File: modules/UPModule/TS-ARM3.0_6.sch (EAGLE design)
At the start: 82 parts, among them IC1 LPC1115, IC100 BD9G101, P1 , P10 , P11 , P12 , P13 , P14 , P2 , P3 , P4 , P5 , P6 , P7 , P8 , P9 , Q1 FA-20H, T1 BC856, T2 BCP52, T3 BC847, X1 EIB

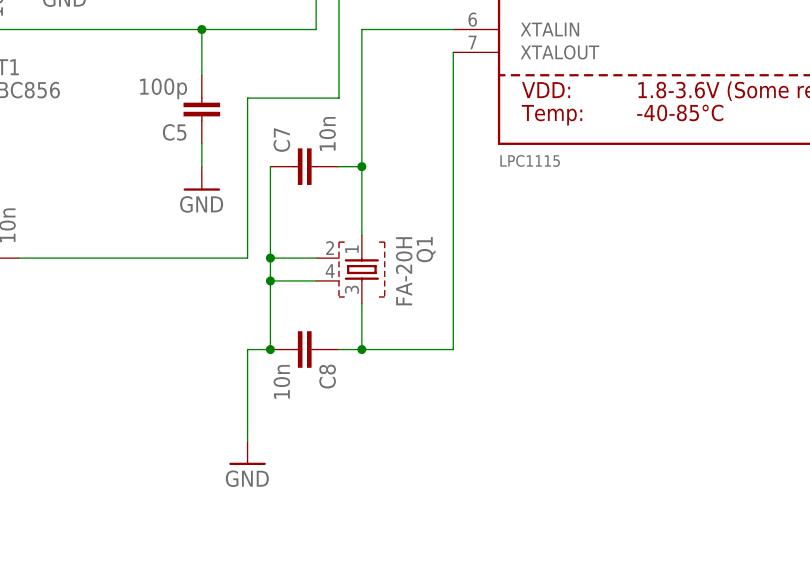
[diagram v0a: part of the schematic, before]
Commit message: Quarz footprint auf ASF geändert
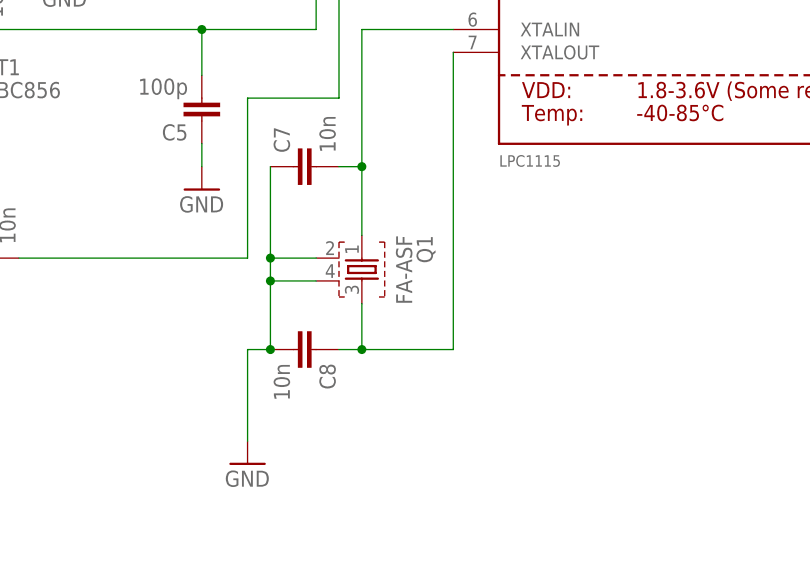
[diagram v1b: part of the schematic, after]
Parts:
- Q1: value FA-20H -> FA-ASF; device crystal:FA-20H -> crystal:FA-ASF
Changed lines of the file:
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@@
 <part name="C7" library="rcl" deviceset="C-EU" device="C1206" value="10n"/>
 <part name="JP10" library="pinhead" deviceset="PINHD-1X1" device=""/>
-<part name="Q1" library="crystal" deviceset="FA-" device="20H" value="FA-20H"/>
+<part name="Q1" library="crystal" deviceset="FA-" device="ASF" value="FA-ASF"/>
 <part name="C8" library="rcl" deviceset="C-EU" device="C1206" value="10n"/>
 </parts>
